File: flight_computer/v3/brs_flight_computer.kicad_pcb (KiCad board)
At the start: 4 copper layers, 81.1 x 75 mm, 251 parts, among them J1 Conn_01x05_Male, J10 Perovskite 3, J11 GaAs Panel, J12 GaAs Temperature, J13 Perovskite 1, J14 Perovskite 2, J15 Power, J16 Power, J18 Power, J19 Power, J2 Conn_01x05_Male, J20 BUSS+, J21 EPS Serial, J22 Power, J3 Conn_01x10_Male, J5 Panel 3, J8 Conn_01x03_Male, J9 0781710004, Q1 BSS138, Q2 BSS138, Q3 BSS138, U1 OPA2387, U10 TLV7031DBV, U11 INA190A4IDDFR, U12 INA190A4IDDFR, U13 INA190A4IDDFR, U14 INA190A4IDDFR, U15 74HC237, U17 INA190A4IDDFR, U18 ADG841YKSZ-500RL7, U19 ADG841YKSZ-500RL7, U2 OPA2387, U20 ADG841YKSZ-500RL7, U21 CD4516B_PW_16, U22 ADG841YKSZ-500RL7, U23 ADG841YKSZ-500RL7, U24 ADG841YKSZ-500RL7, U25 ADG841YKSZ-500RL7, U26 CD4516B_PW_16, U27 ADG841YKSZ-500RL7, U28 ADG841YKSZ-500RL7, U29 ADG841YKSZ-500RL7, U3 TLV7031DBV, U30 ADG841YKSZ-500RL7, U31 CD4516B_PW_16, U32 ADG841YKSZ-500RL7, U33 ADG841YKSZ-500RL7, U34 ADG841YKSZ-500RL7, U35 ADG841YKSZ-500RL7, U36 CD4516B_PW_16, U37 ADG841YKSZ-500RL7, U38 CD4518BM96, U4 74HC237, U42 ADG839YKSZ-REEL7, U43 ADG839YKSZ-REEL7, U44 ADG839YKSZ-REEL7, U45 ADG839YKSZ-REEL7, U46 ADG839YKSZ-REEL7, U47 ADG839YKSZ-REEL7, U48 ADG839YKSZ-REEL7, U49 ADG839YKSZ-REEL7, U5 74HC237, U50 ADG839YKSZ-REEL7, U51 ADG839YKSZ-REEL7, U52 ADG839YKSZ-REEL7, U53 ADG839YKSZ-REEL7, U54 ADG839YKSZ-REEL7, U55 ADG839YKSZ-REEL7, U56 ADG839YKSZ-REEL7, U57 ADG839YKSZ-REEL7, U58 ADG839YKSZ-REEL7, U59 ADG839YKSZ-REEL7, U6 4012, U7 LT6654AHS6-3.3, U8 MSP430FR5969IRGZR, U9 SN74CBT3253, Y1 CM8V-T1A

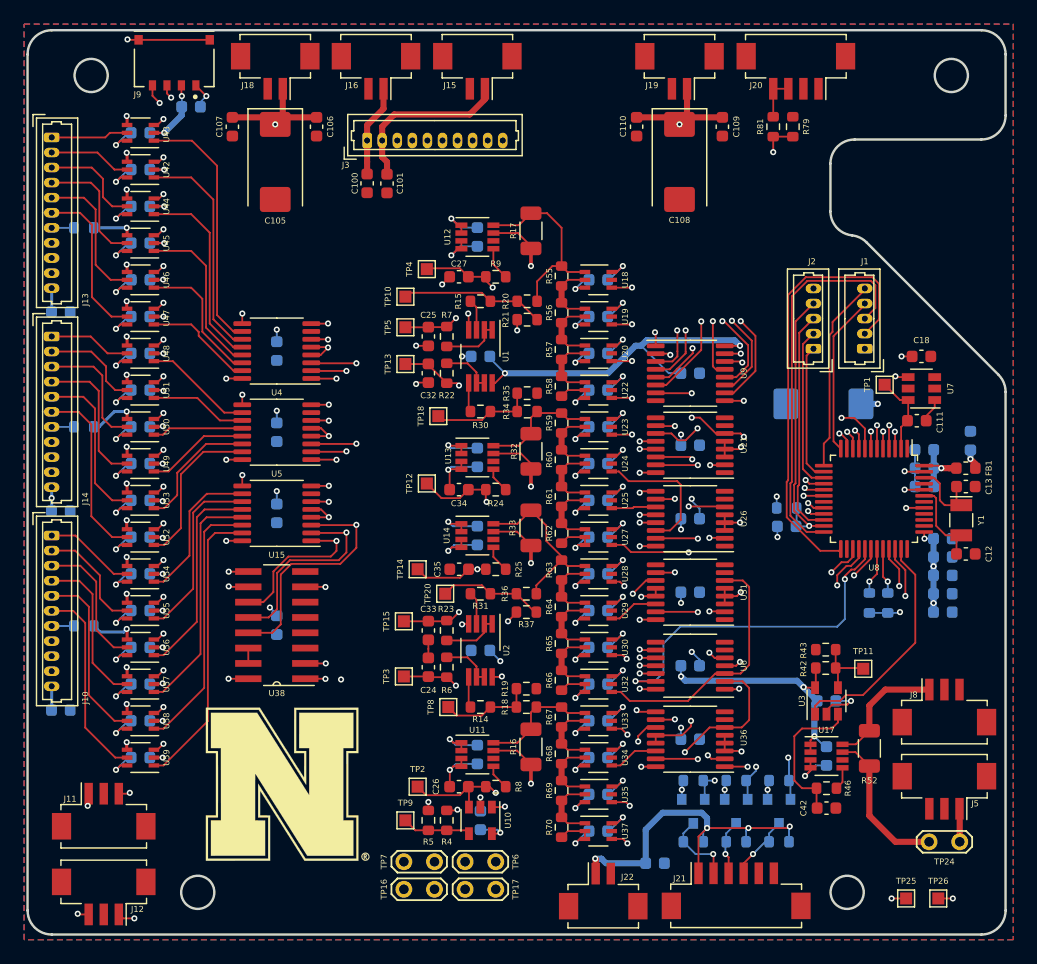
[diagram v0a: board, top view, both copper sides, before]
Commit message: Updating based on harnesses
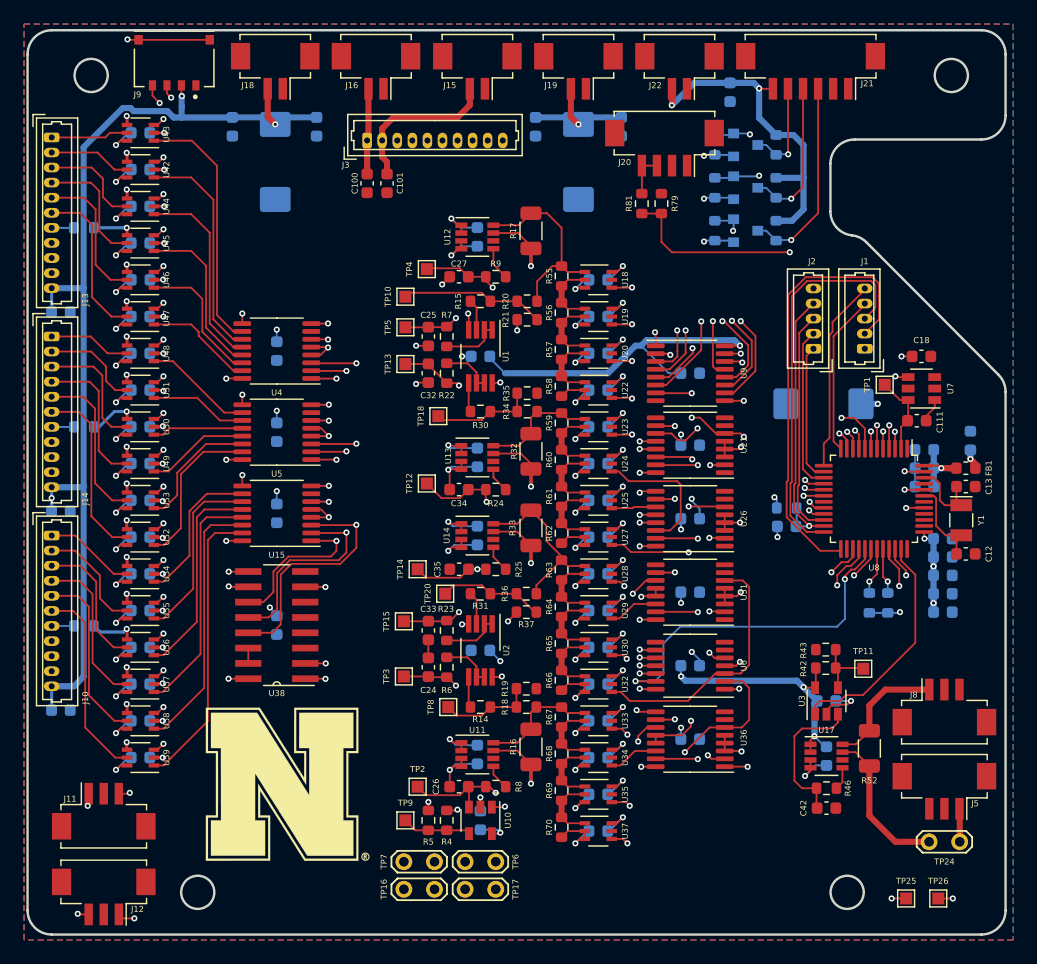
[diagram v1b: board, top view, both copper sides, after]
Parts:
- removed C48: 1u, Capacitor_SMD:C_0603_1608Metric
- C105, C106, C107, C108, C109, C110: moved to B.Cu
- moved J22 68.3 mm to (167.4, 73.5), turned to 180 degrees
- moved J21 68.3 mm to (178.3, 73.5), turned to 180 degrees
- moved C104 64.2 mm to (171.6, 75.2), turned to 270 degrees
- moved R80 58.2 mm to (175.4, 79.6), turned to 90 degrees
- moved Q3 55.4 mm to (172.9, 79.6), turned to 0 degrees
- moved R77 54.3 mm to (175.4, 83.2), turned to 90 degrees
- moved R78 52.7 mm to (170.3, 79.6), turned to 270 degrees
- moved Q2 51.7 mm to (172.9, 83.2), turned to 0 degrees
- moved R75 50.7 mm to (175.4, 86.7), turned to 90 degrees
- moved R76 49.2 mm to (170.3, 83.2), turned to 270 degrees
- moved Q1 48.2 mm to (172.9, 86.7), turned to 0 degrees
- moved R74 45.9 mm to (170.3, 86.7), turned to 270 degrees
- moved J20 12.6 mm to (166.1, 79.9)
- moved R81 12.6 mm to (164.3, 84.5)
- moved R79 12.6 mm to (165.9, 84.5)
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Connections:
- C30 pad 1: VBUS -> +3V3
- C74 pad 1: VBUS -> +3V3
- C75 pad 1: VBUS -> +3V3
- C76 pad 1: VBUS -> +3V3
- C77 pad 1: VBUS -> +3V3
- C79 pad 1: VBUS -> +3V3
- C80 pad 1: VBUS -> +3V3
- C81 pad 1: VBUS -> +3V3
- C82 pad 1: VBUS -> +3V3
- C83 pad 1: VBUS -> +3V3
- C84 pad 1: VBUS -> +3V3
- C85 pad 1: VBUS -> +3V3
- C86 pad 1: VBUS -> +3V3
- C88 pad 1: VBUS -> +3V3
- C89 pad 1: VBUS -> +3V3
- C90 pad 1: VBUS -> +3V3
- C91 pad 1: VBUS -> +3V3
- C92 pad 1: VBUS -> +3V3
- C93 pad 1: VBUS -> +3V3
- C96 pad 1: VBUS -> +3V3
- C97 pad 1: VBUS -> +3V3
- C99 pad 1: VBUS -> +3V3
- J15 pad 1: VPP -> GND
- J15 pad 2: GND -> VPP
- J16 pad 1: VDDF -> GND
- J16 pad 2: GND -> VDDF
- J18 pad 1: VBUS -> GND
- J18 pad 2: GND -> VBUS
- J19 pad 1: +3V3 -> GND
- J19 pad 2: GND -> +3V3
- J21 pad 1: +5V -> Net-(J21-Pad1)
- J21 pad 2: Net-(J21-Pad2) -> GND
- J21 pad 5: GND -> Net-(J21-Pad5)
- J21 pad 6: Net-(J21-Pad6) -> +5V
- J22 pad 1: +5V -> GND
- J22 pad 2: GND -> +5V
- Q1 pad 3: Net-(J21-Pad4) -> Net-(J21-Pad3)
- Q2 pad 3: Net-(J21-Pad3) -> Net-(J21-Pad4)
- Q3 pad 3: Net-(J21-Pad2) -> Net-(J21-Pad5)
- R75 pad 1: Net-(J21-Pad4) -> Net-(J21-Pad3)
- R77 pad 1: Net-(J21-Pad3) -> Net-(J21-Pad4)
- R80 pad 1: Net-(J21-Pad2) -> Net-(J21-Pad5)
- U1 pad 8: +3V3 -> VBUS
- U15 pad 16: VBUS -> +3V3
- U15 pad 6: VBUS -> +3V3
- U2 pad 8: VBUS -> +3V3
- U38 pad 1: VBUS -> +3V3
- U38 pad 10: VBUS -> +3V3
- U38 pad 16: VBUS -> +3V3
- U38 pad 7: VBUS -> +3V3
- U4 pad 16: VBUS -> +3V3
- U4 pad 6: VBUS -> +3V3
- U42 pad 2: VBUS -> +3V3
- U43 pad 2: VBUS -> +3V3
- U44 pad 2: VBUS -> +3V3
- U45 pad 2: VBUS -> +3V3
- U46 pad 2: VBUS -> +3V3
- U47 pad 2: VBUS -> +3V3
- U48 pad 2: VBUS -> +3V3
- U49 pad 2: VBUS -> +3V3
- U5 pad 16: VBUS -> +3V3
- U5 pad 6: VBUS -> +3V3
- U50 pad 2: VBUS -> +3V3
- U51 pad 2: VBUS -> +3V3
- U52 pad 2: VBUS -> +3V3
- U53 pad 2: VBUS -> +3V3
- U54 pad 2: VBUS -> +3V3
- U55 pad 2: VBUS -> +3V3
- U56 pad 2: VBUS -> +3V3
- U57 pad 2: VBUS -> +3V3
- U58 pad 2: VBUS -> +3V3
- U59 pad 2: VBUS -> +3V3
- U6 pad 12: VBUS -> +3V3
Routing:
- net +3V3: track 90.2 -> 146.9 mm, vias 25 -> 58
- net /EPS Connections/BUSY: track 28.9 -> 43.7 mm
- net Net-(J21-Pad3): track 4.62 -> 16.6 mm
- net VBUS: track 154.4 -> 164.1 mm, vias 63 -> 30
- net Net-(J21-Pad5): track 0.00 -> 8.33 mm, vias 0 -> 1
- net Net-(J21-Pad4): track 5.54 -> 12.7 mm
- net Net-(J21-Pad2): track 6.37 -> 0.00 mm, vias 1 -> 0
- net /EPS Connections/RX: track 32.2 -> 37.8 mm
- net /EPS Connections/TX: track 28.9 -> 34.3 mm
- net /EPS Connections/READ_BUSS: track 32.9 -> 36.2 mm
- net GND: track 229.0 -> 226.7 mm, vias 101 -> 100
- net +5V: track 29.8 -> 28.1 mm, vias 4 -> 2
- net VPP: track 14.4 -> 13.4 mm
- net VDDF: track 7.64 -> 7.12 mm
- net /Ground Switcher/MUX_CLOCK: vias 3 -> 2
- removed copper zone on In1.Cu, net VBUS

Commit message: Integrating flight computer
- EPS commands tested and working
- Updated v3, fixing connector polarity
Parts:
- added R10: 4k7, Resistor_SMD:R_0603_1608Metric, F.Cu at (138.2, 142.9)
- R18: value 10M -> 3M
- R19, R20, R21, R34, R35, R36, R37: value 10M -> 1M
- moved TP24 2.55 mm to (188.1, 137.6)
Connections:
- J11 pad 1: /Curve Tracer/GAAS_POS -> GND
- J11 pad 3: GND -> /Curve Tracer/GAAS_POS
- J12 pad 1: /Ground Switcher/GAAS_TEMP -> +3V3
- J12 pad 2: Net-(J12-Pad2) -> /Ground Switcher/GAAS_TEMP
- J12 pad 3: GND -> Net-(J12-Pad3)
- J5 pad 1: Net-(J5-Pad1) -> GND
- J5 pad 3: GND -> Net-(J5-Pad3)
- J8 pad 1: Net-(J8-Pad1) -> GND
- J8 pad 3: GND -> Net-(J8-Pad3)
- R52 pad 1: Net-(J8-Pad1) -> Net-(J8-Pad3)
- TP24 pad 1: Net-(J5-Pad1) -> Net-(J5-Pad3)
- U17 pad 8: Net-(J8-Pad1) -> Net-(J8-Pad3)
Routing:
- net Net-(J8-Pad3): track 0.00 -> 14.9 mm
- net Net-(J8-Pad1): track 10.3 -> 0.00 mm
- net Net-(J5-Pad3): track 0.00 -> 2.94 mm
- net Net-(J5-Pad1): track 2.75 -> 0.00 mm
- net /Ground Switcher/GAAS_TEMP: track 89.7 -> 92.4 mm
- net Net-(R52-Pad2): track 12.7 -> 10.2 mm
- net +3V3: track 146.9 -> 149.1 mm, vias 58 -> 60
- net /Curve Tracer/GAAS_POS: track 36.3 -> 34.3 mm
- net P1_CP: track 81.0 -> 80.1 mm
- net GND: track 226.7 -> 226.0 mm, vias 100 -> 99

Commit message: Integrating flight computer
- Update FSS100 connector
- Update secondary payload connector
- Add pullup resistor to GaAs data
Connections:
- J9 pad 1: GND -> /Ground Switcher/SDA
- J9 pad 2: VBUS -> /Ground Switcher/SCL
- J9 pad 3: /Ground Switcher/SCL -> VBUS
- J9 pad 4: /Ground Switcher/SDA -> GND
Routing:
- net GND: track 226.0 -> 229.2 mm
- net VBUS: track 164.1 -> 166.3 mm
- net /Ground Switcher/SDA: track 155.0 -> 156.9 mm

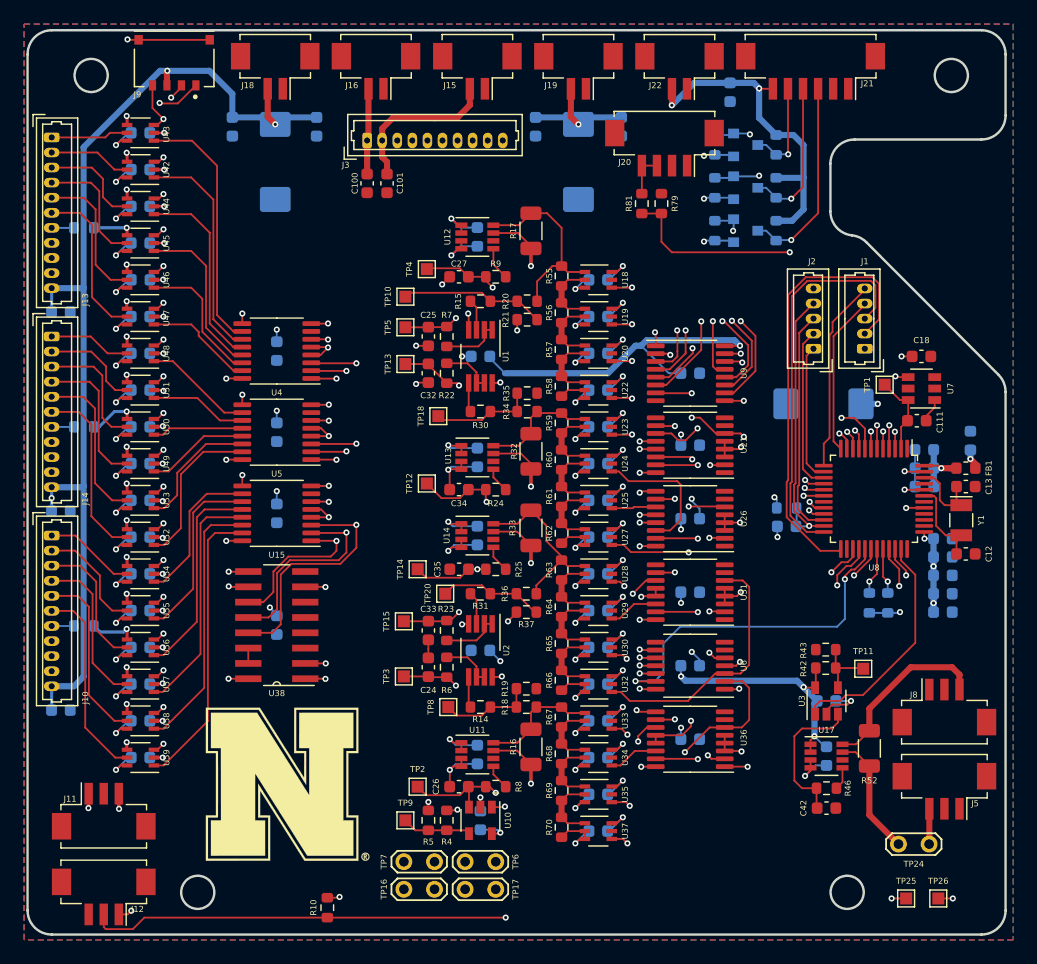
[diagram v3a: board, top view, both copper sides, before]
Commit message: Add silkscreen text
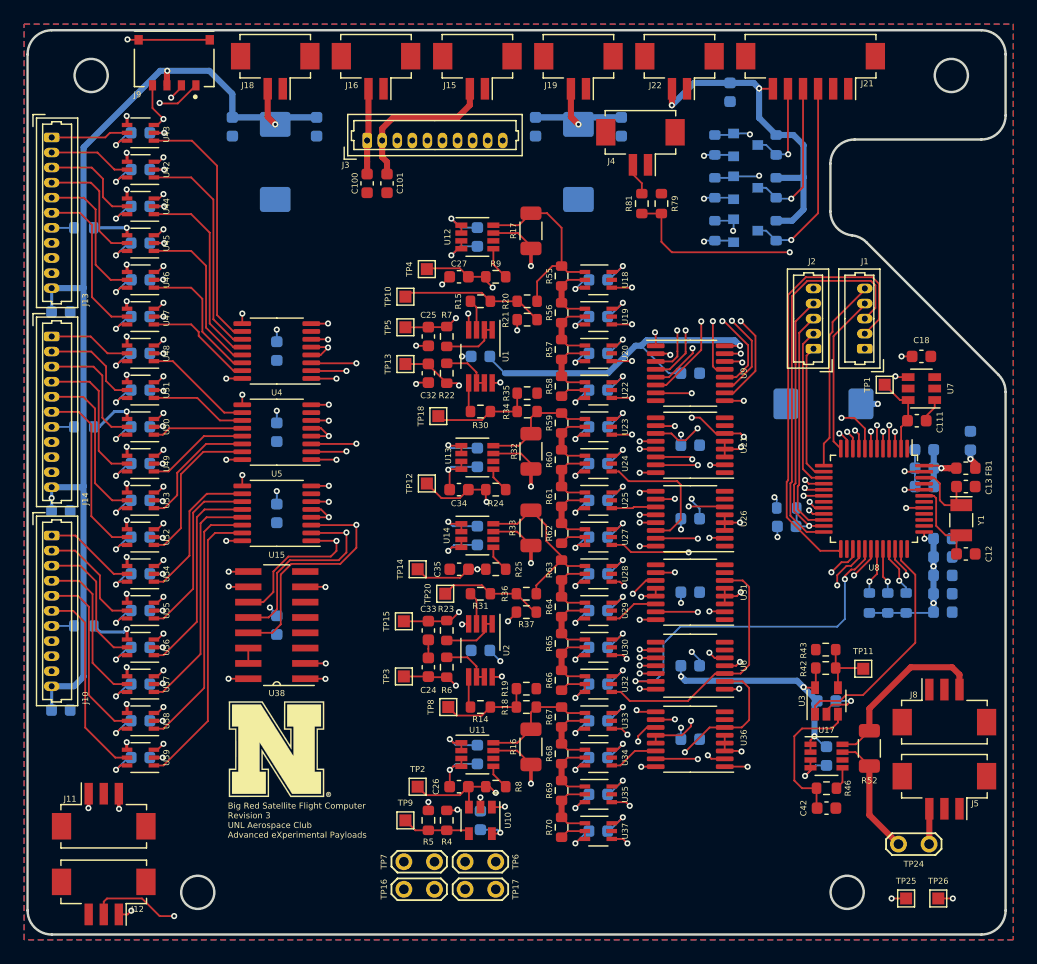
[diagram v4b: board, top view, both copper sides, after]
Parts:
- removed J20: BUSS+, Connector_Hirose:Hirose_DF13C_CL535-0404-8-51_1x04-1MP_P1.25mm_Vertical
- added J4: BUSS, Connector_Hirose:Hirose_DF13C_CL535-0402-2-51_1x02-1MP_P1.25mm_Vertical, F.Cu at (164.1, 79.8)
- R10: moved to B.Cu
- moved R10 54.3 mm to (186.2, 117.6), turned to 270 degrees
- moved G*** 2.95 mm to (134.0, 129.7)
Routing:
- net /Ground Switcher/GAAS_TEMP: track 92.4 -> 94.8 mm
- net +3V3: track 149.1 -> 150.9 mm, vias 60 -> 58
- net Net-(J4-Pad2): track 3.57 -> 2.69 mm
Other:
- board text added: "Big Red Satellite Flight Computer Revision 3 UNL Aerospace Club Advanced eXperimental Payloads"

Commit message: Fix some tracks and update firmware
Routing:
- net /Microcontroller/CT_GOOD: track 18.5 -> 19.1 mm

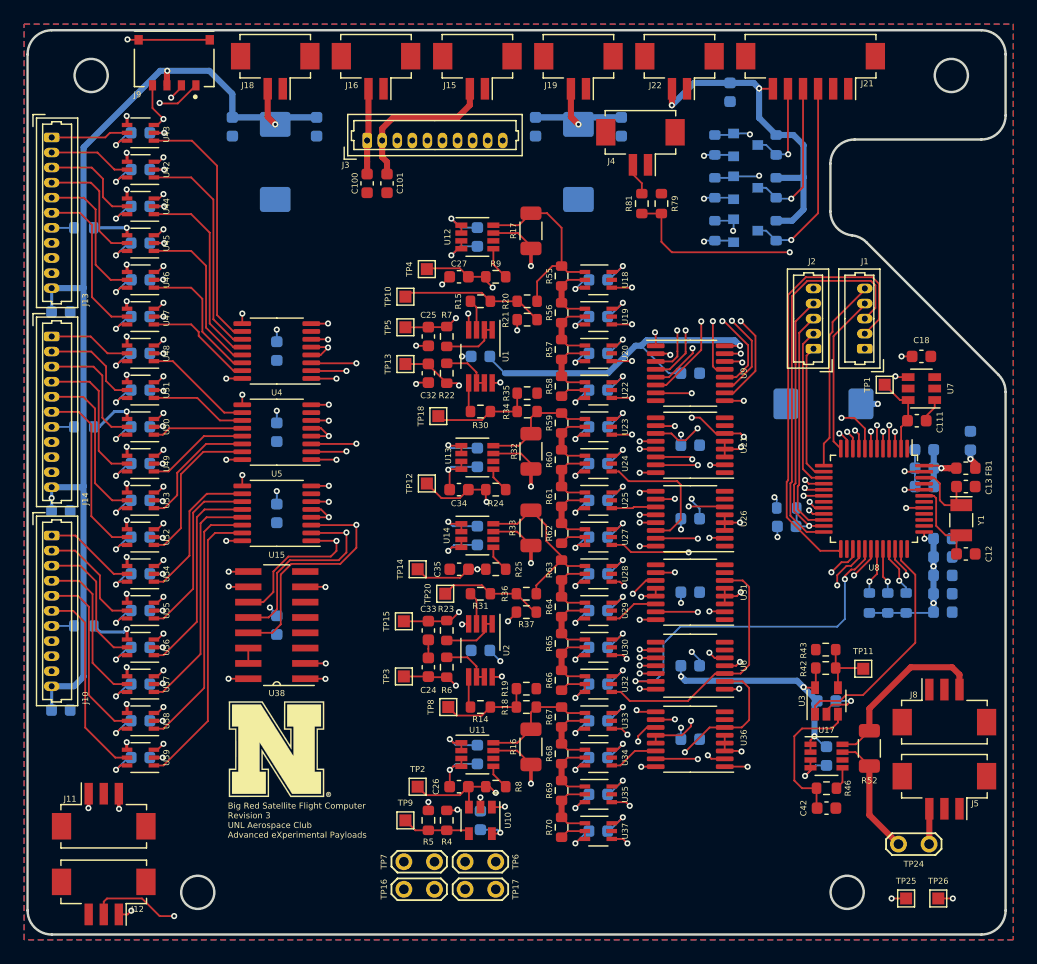
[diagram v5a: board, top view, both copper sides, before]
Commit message: Update hardware
- Add separate discharge resistance paths to flight computer
- Update footprint for payload holder
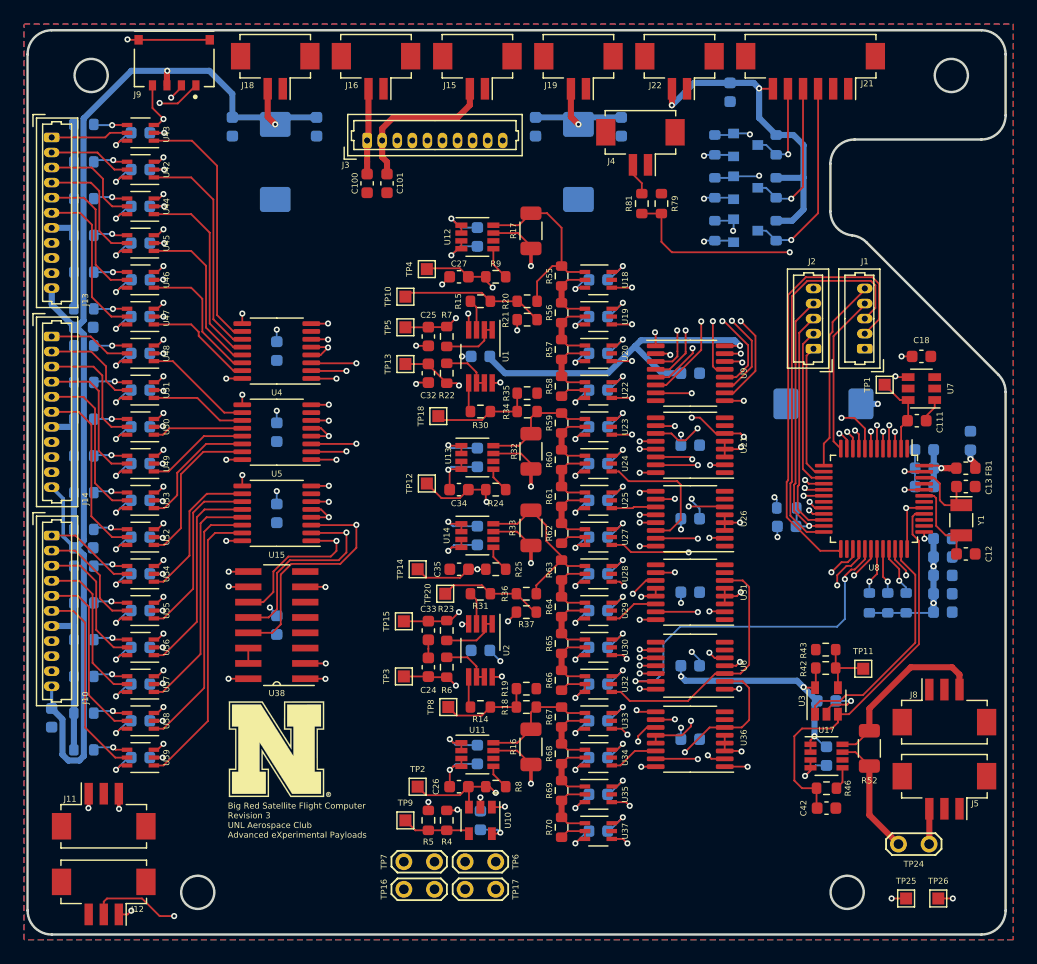
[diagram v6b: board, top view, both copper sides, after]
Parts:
- added R11: 400, Resistor_SMD:R_0603_1608Metric, B.Cu at (118.0, 93.2)
- added R12: 400, Resistor_SMD:R_0603_1608Metric, B.Cu at (118.0, 90.2)
- added R13: 400, Resistor_SMD:R_0603_1608Metric, B.Cu at (118.0, 87.1)
- added R26: 400, Resistor_SMD:R_0603_1608Metric, B.Cu at (118.0, 84.1)
- added R27: 400, Resistor_SMD:R_0603_1608Metric, B.Cu at (118.0, 81.0)
- added R28: 400, Resistor_SMD:R_0603_1608Metric, B.Cu at (118.0, 111.5)
- added R29: 400, Resistor_SMD:R_0603_1608Metric, B.Cu at (118.0, 108.5)
- added R38: 400, Resistor_SMD:R_0603_1608Metric, B.Cu at (118.0, 105.4)
- added R39: 400, Resistor_SMD:R_0603_1608Metric, B.Cu at (118.0, 102.4)
- added R40: 400, Resistor_SMD:R_0603_1608Metric, B.Cu at (118.0, 99.3)
- added R41: 400, Resistor_SMD:R_0603_1608Metric, B.Cu at (118.0, 129.8)
- added R44: 400, Resistor_SMD:R_0603_1608Metric, B.Cu at (118.0, 126.7)
- added R45: 400, Resistor_SMD:R_0603_1608Metric, B.Cu at (118.0, 123.7)
- added R47: 400, Resistor_SMD:R_0603_1608Metric, B.Cu at (118.0, 120.7)
- added R48: 400, Resistor_SMD:R_0603_1608Metric, B.Cu at (118.0, 117.6)
- R71, R72, R73: value 10k -> 400
- moved R71 8.57 mm to (118.0, 77.9)
- moved R72 6.73 mm to (118.0, 96.3)
- moved R73 4.95 mm to (118.0, 114.6)
- moved C17 3.59 mm to (118.0, 113.0)
- moved C28 2.29 mm to (118.0, 94.7)
- moved C29 0.99 mm to (115.3, 127.1), turned to 270 degrees
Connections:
- C42 pad 1: Net-(C42-Pad1) -> /Microcontroller/PANEL_3_CURRENT_V
- R46 pad 1: Net-(C42-Pad1) -> /Microcontroller/PANEL_3_CURRENT_V
- U3 pad 3: Net-(C42-Pad1) -> /Microcontroller/PANEL_3_CURRENT_V
- U42 pad 4: Net-(R71-Pad2) -> Net-(R27-Pad2)
- U44 pad 4: Net-(R71-Pad2) -> Net-(R26-Pad2)
- U45 pad 4: Net-(R71-Pad2) -> Net-(R13-Pad2)
- U46 pad 4: Net-(R71-Pad2) -> Net-(R12-Pad2)
- U47 pad 4: Net-(R71-Pad2) -> Net-(R11-Pad2)
- U49 pad 4: Net-(R72-Pad2) -> Net-(R38-Pad2)
- U50 pad 4: Net-(R72-Pad2) -> Net-(R39-Pad2)
- U51 pad 4: Net-(R72-Pad2) -> Net-(R40-Pad2)
- U52 pad 4: Net-(R72-Pad2) -> Net-(R28-Pad2)
- U53 pad 4: Net-(R72-Pad2) -> Net-(R29-Pad2)
- U55 pad 4: Net-(R73-Pad2) -> Net-(R48-Pad2)
- U56 pad 4: Net-(R73-Pad2) -> Net-(R47-Pad2)
- U57 pad 4: Net-(R73-Pad2) -> Net-(R45-Pad2)
- U58 pad 4: Net-(R73-Pad2) -> Net-(R44-Pad2)
- U59 pad 4: Net-(R73-Pad2) -> Net-(R41-Pad2)
- U8 pad 40: Net-(U8-Pad40) -> /Microcontroller/PANEL_3_CURRENT_V
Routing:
- net /Microcontroller/PANEL_3_CURRENT_V: track 0.00 -> 33.2 mm
- net Net-(R73-Pad2): track 23.0 -> 2.88 mm, vias 6 -> 1
- net Net-(R72-Pad2): track 22.8 -> 2.77 mm, vias 6 -> 1
- net Net-(R71-Pad2): track 22.3 -> 2.80 mm, vias 6 -> 1
- net P1_CP: track 80.1 -> 95.4 mm
- net P2_CP: track 65.9 -> 81.2 mm
- net P3_CP: track 55.7 -> 71.0 mm
- net VBUS: track 166.3 -> 179.6 mm, vias 30 -> 29
- net Net-(C42-Pad1): track 12.2 -> 0.00 mm
- net GND: track 229.2 -> 232.6 mm
- net Net-(R41-Pad2): track 0.00 -> 2.93 mm, vias 0 -> 1
- net Net-(R45-Pad2): track 0.00 -> 2.91 mm, vias 0 -> 1
- net Net-(R44-Pad2): track 0.00 -> 2.91 mm, vias 0 -> 1
- net Net-(R47-Pad2): track 0.00 -> 2.88 mm, vias 0 -> 1
- net Net-(R28-Pad2): track 0.00 -> 2.88 mm, vias 0 -> 1
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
